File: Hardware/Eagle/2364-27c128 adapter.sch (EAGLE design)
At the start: 4 parts, among them IC1 27C128P

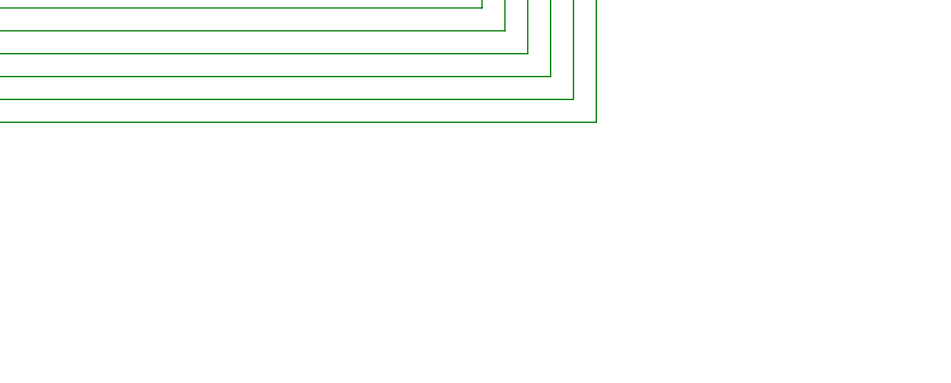
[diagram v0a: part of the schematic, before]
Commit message: Update Hardware/Eagle/2364-27c128 adapter.sch
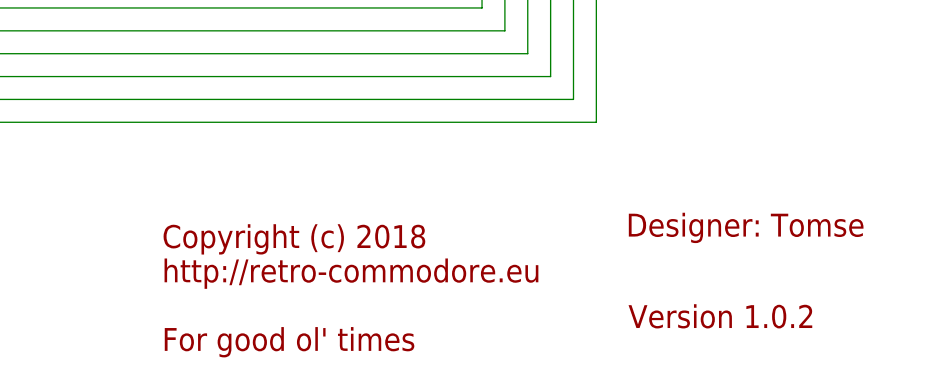
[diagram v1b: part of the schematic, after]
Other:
- note added: "Copyright (c) 2018 http://retro-commodore.eu For good ol' times"
- note added: "Designer: Tomse"
- note added: "Version 1.0.2"
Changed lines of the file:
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@@
 <part name="SUPPLY1" library="supply2" library_urn="urn:adsk.eagle:library:372" deviceset="VCC" device=""/>
 <part name="SUPPLY2" library="supply2" library_urn="urn:adsk.eagle:library:372" deviceset="VCC" device=""/>
+<part name="FRAME1" library="frames" library_urn="urn:adsk.eagle:library:229" deviceset="A4L-LOC" device=""/>
 </parts>
 <sheets>
 <sheet>
 <plain>
+<text x="104.14" y="-25.4" size="2.54" layer="94">Copyright (c) 2018
+http://retro-commodore.eu
+For good ol' times</text>
+<text x="155.956" y="-22.86" size="2.54" layer="94">Version 1.0.2</text>
+<text x="155.702" y="-12.7" size="2.54" layer="94">Designer: Tomse</text>
 </plain>
 <instances>
@@
 <instance part="SUPPLY1" gate="G$1" x="30.48" y="25.4"/>
 <instance part="SUPPLY2" gate="G$1" x="106.68" y="101.6"/>
+<instance part="FRAME1" gate="G$1" x="-60.96" y="-33.02" smashed="yes">
+<attribute name="DRAWING_NAME" x="156.21" y="-17.78" size="2.54" layer="94"/>
+<attribute name="SHEET" x="169.545" y="-27.94" size="2.54" layer="94"/>
+</instance>
 </instances>
 <busses>
@@
 </drawing>
 <compatibility>
+<note version="6.3" minversion="6.2.2" severity="warning">
+Since Version 6.2.2 text objects can contain more than one line,
+which will not be processed correctly with this version.
+</note>
 <note version="8.2" severity="warning">
 Since Version 8.2, EAGLE supports online libraries. The ids
